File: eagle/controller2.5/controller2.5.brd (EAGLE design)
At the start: 63.5 x 45.7 mm, 46 parts, among them Q2 2N2907, U1 ATMEGA328P

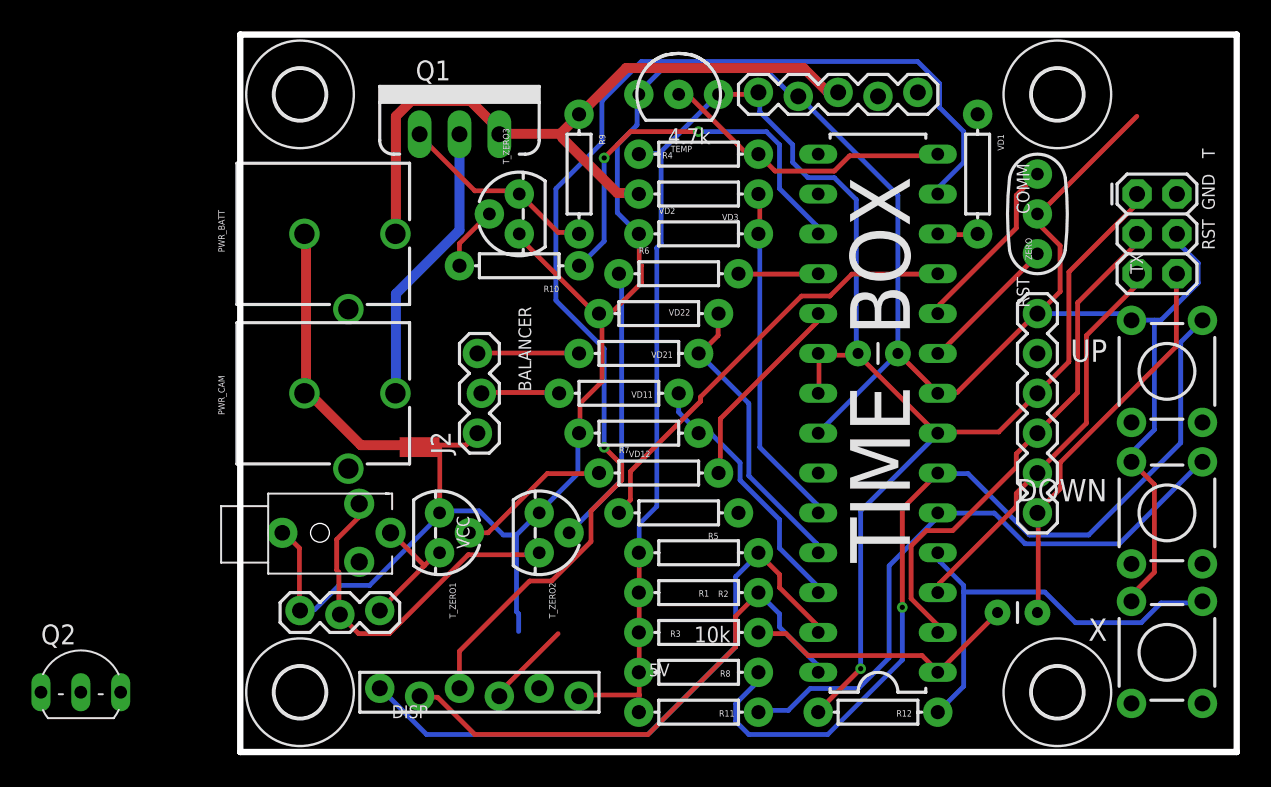
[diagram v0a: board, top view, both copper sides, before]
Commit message: controller2.5: smaller board
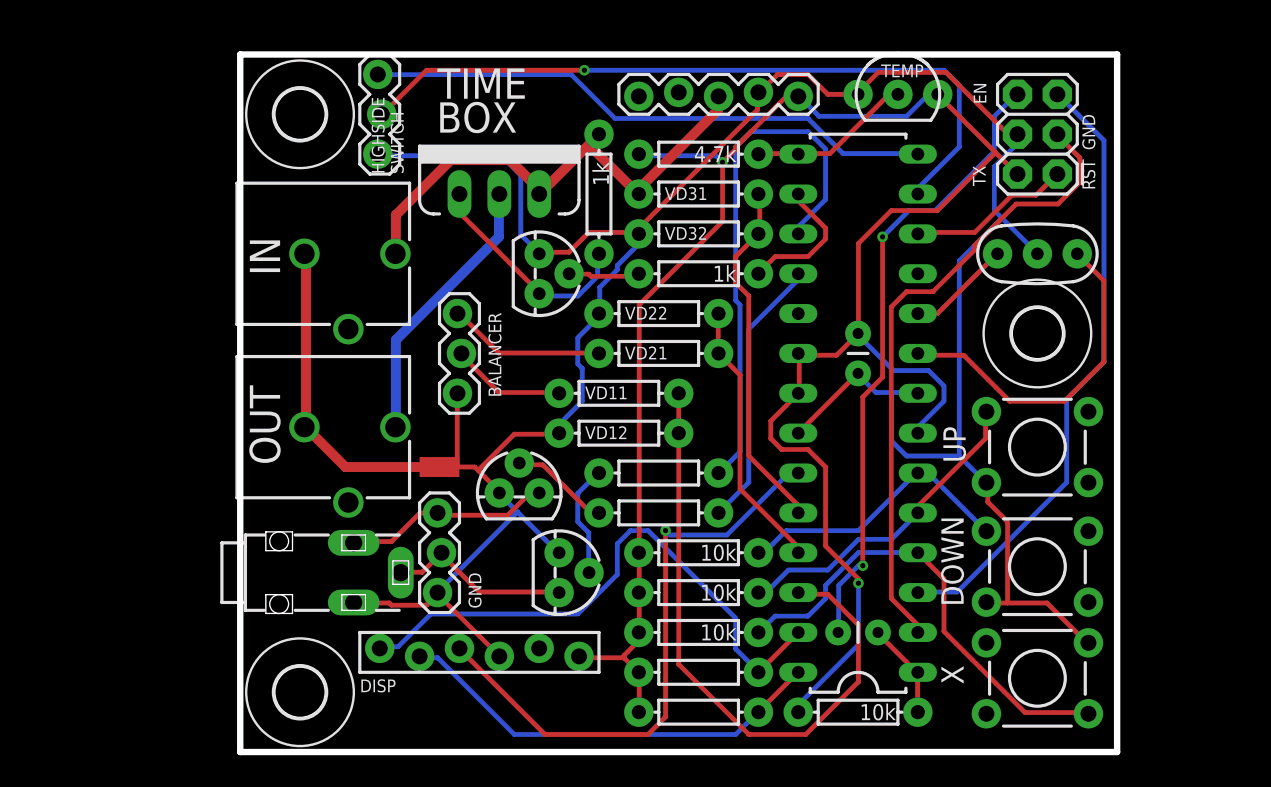
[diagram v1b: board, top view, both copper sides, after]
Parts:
- removed COMM: (no value), SparkFun-Connectors:FTDI_BASIC
- removed H2: MOUNT-HOLE3.2, holes:3,2
- removed J1: (no value), SparkFun-Connectors:STEREOJACK2.5MM_STEREOJACK2.5MM
- removed Q1: (no value), SparkFun-DiscreteSemi:TO220V
- removed Q2: 2N2907, adafruit:TO92-EBC-OVAL
- removed R11, R12, R5, R8, VD1: (no value), SparkFun-Resistors:AXIAL-0.3
- removed T_ZERO1, T_ZERO2, T_ZERO3: (no value), SparkFun-DiscreteSemi:TO-92
- added HIGHSIDESWITCH: (no value), SparkFun-DiscreteSemi:TO220V
- added RB1, RB2, RB3: 10k, SparkFun-Resistors:AXIAL-0.3
- added SOFT_SERIAL: (no value), SparkFun-Connectors:1X03_LOCK
- added T_CAM1, T_CAM2, T_HSS: (no value), SparkFun-DiscreteSemi:TO-92
- added X1: 1501_04, con-lumberg:1501_05
- R10, R9: value (none) -> 1k
- ZERO: value FEMALE 2x3 -> (none)
- moved H3 15.3 mm to (50.8, 26.7)
- moved BTN_UP 14.9 mm to (50.8, 11.8), turned to 180 degrees
- moved TEMP 14.0 mm to (41.9, 41.9)
- moved R6 12.8 mm to (26.7, 17.8)
- moved C1 12.8 mm to (38.1, 7.62), turned to 0 degrees
- moved R10 11.4 mm to (29.2, 30.5)
- moved R3 11.4 mm to (39.4, 2.54)
- moved BTN_DW 9.26 mm to (50.8, 19.4), turned to 180 degrees
- moved SHTR 8.98 mm to (12.7, 10.2), turned to 90 degrees
- moved BTN_X 8.42 mm to (50.8, 4.70), turned to 0 degrees
- moved R2 7.62 mm to (29.2, 2.54)
- moved R1 7.62 mm to (29.2, 5.08)
- moved ZERO 5.24 mm to (52.1, 36.8), turned to 90 degrees
- moved C3 2.84 mm to (39.4, 24.1), turned to 90 degrees
- moved J2 2.84 mm to (14.0, 22.9)
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- renumbered R4 to RTEMP, VD2 to VD32, VD3 to VD31
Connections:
- removed net EXT_EN: U1.15
- removed net FOO: U1.23
- removed net N$12: Q2.C, ZERO.1
- removed net N$4: Q2.B, VD1.P$1
- removed net N$6: DISP.4
- new net FOO2: U1.19
- new net SOFT_RX: SOFT_SERIAL.3, U1.14
- new net SOFT_TX: SOFT_SERIAL.2, U1.13
- net BATT_VCC: now also HIGHSIDESWITCH.3; no longer Q1.3
- net BTN1: now also RB1.P$1; no longer R8.P$1
- net BTN2: now also RB2.P$1; no longer R11.P$1
- net BTN3: now also RB3.P$1; no longer R12.P$1
- net CAM1: now also U1.18; no longer U1.19
- net CAM2: now also U1.17; no longer U1.18
- net CAM_EN: now also U1.16; no longer U1.17
- net CAM_OUT: now also HIGHSIDESWITCH.2; no longer Q1.2
- net DISP_RST: now also U1.23; no longer U1.13
- net GND: now also DISP.4, SOFT_SERIAL.1, T_CAM1.1, T_CAM2.1, T_HSS.1, X1.1; no longer COMM.GND, J1.SHIELD, T_ZERO1.1, T_ZERO2.1, T_ZERO3.1
- net N$10: now also T_CAM1.3, X1.3; no longer J1.TIP, T_ZERO1.3
- net N$11: now also T_CAM2.2; no longer T_ZERO2.2
- net N$13: now also T_HSS.2; no longer T_ZERO3.2
- net N$14: now also HIGHSIDESWITCH.1, T_HSS.3; no longer Q1.1, T_ZERO3.3
- net N$3: now also T_CAM1.2; no longer T_ZERO1.2
- net N$7: now also T_CAM2.3, X1.2; no longer J1.RING, T_ZERO2.3
- net RST: no longer COMM.DTR
- net RX: no longer COMM.TXO
- net TEMP: now also U1.15; no longer U1.14
- net TX: no longer COMM.RXI
- net VCC: now also RB1.P$2, RB2.P$2, RB3.P$2; no longer COMM.VCC, Q2.E, R11.P$2, R12.P$2, R8.P$2
- net ZERO_EN: now also ZERO.1; no longer VD1.P$2
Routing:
- net SOFT_TX: track 0.00 -> 46.4 mm, vias 0 -> 1
- net BTN1: track 57.4 -> 18.1 mm, vias 1 -> 0
- net DISP_RST: track 77.0 -> 38.0 mm
- net SOFT_RX: track 0.00 -> 36.5 mm
- net CAM2: track 5.09 -> 34.2 mm
- net DISP_EN: track 27.8 -> 0.00 mm
- net CELL1: track 16.8 -> 40.3 mm
- net BTN2: track 40.2 -> 20.5 mm
- net CAM_EN: track 26.5 -> 8.79 mm, vias 2 -> 0
- net RST: track 25.3 -> 40.2 mm, vias 0 -> 2
- net TX: track 25.6 -> 39.3 mm
- net BATT_VCC: track 46.1 -> 33.1 mm
- net N$9: track 9.07 -> 21.7 mm
- net N$1: track 17.9 -> 6.18 mm
- net N$7: track 23.1 -> 11.7 mm
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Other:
- board size 63.5 x 45.7 mm -> 55.9 x 44.5 mm
- board text added: "EN"
- board text added: "HIGHSIDE SWITCH"
- board text added: "IN"
- board text added: "OUT"
- board text added: "TEMP"
- board text added: "VD11"
- board text added: "VD12"
- board text added: "VD21"
- board text added: "VD22"
- board text added: "VD31"
- board text added: "VD32"
- board text removed: "5V"
- board text removed: "COMM"
- board text removed: "T"
- board text removed: "VCC"

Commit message: controller2.5: production version
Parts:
- moved SOFT_SERIAL 36.9 mm to (45.7, 36.8)
- moved RTEMP 18.2 mm to (45.7, 30.5), turned to 90 degrees
- moved C1 7.18 mm to (43.2, 2.54), turned to 180 degrees
- moved R3 5.08 mm to (34.3, 2.54)
- moved C3 3.81 mm to (39.4, 27.9), turned to 270 degrees
- moved VD22 3.59 mm to (29.2, 30.5)
- moved R10 2.54 mm to (29.2, 33.0)
- moved VD21 2.54 mm to (26.7, 27.9)
- moved R7 2.54 mm to (26.7, 17.8)
- moved RB1 2.54 mm to (29.2, 15.2)
- moved R1 2.54 mm to (29.2, 7.62)
- moved R2 2.54 mm to (29.2, 5.08)
- moved RB3 2.54 mm to (29.2, 10.2)
- moved R6 2.54 mm to (26.7, 20.3)
- moved RB2 2.54 mm to (29.2, 12.7)
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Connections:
- removed net DISP_EN: U1.11
- removed net FOO2: U1.19
- net CAM2: now also U1.16; no longer U1.17
- net CAM_EN: now also U1.17; no longer U1.16
- net SOFT_TX: now also U1.15; no longer U1.13
- net TEMP: now also U1.13; no longer U1.15
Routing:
- net VCC: track 130.9 -> 80.8 mm, vias 2 -> 0
- net TX: track 39.3 -> 87.2 mm
- net SOFT_TX: track 46.4 -> 10.9 mm, vias 1 -> 0
- net SOFT_RX: track 36.5 -> 4.88 mm
- net CAM2: track 34.2 -> 19.8 mm
- net RST: track 40.2 -> 51.4 mm, vias 2 -> 0
- net BTN3: track 29.8 -> 19.6 mm
- net TEMP: track 10.5 -> 20.7 mm
- net N$9: track 21.7 -> 11.8 mm
- net VD_DIRECT: track 22.6 -> 30.4 mm
- net N$8: track 6.65 -> 13.4 mm
- net CAM_EN: track 8.79 -> 2.57 mm
- net CELL2: track 17.4 -> 23.5 mm, vias 0 -> 1
- net GND: track 169.9 -> 175.4 mm
- net DISP_RST: track 38.0 -> 32.5 mm, vias 1 -> 0
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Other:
- board text added: "RX"
- board text added: "VIN"

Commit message: controller2.5: last minor changes for production
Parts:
- moved CONV_X_VCC 1.27 mm to (34.3, 41.9)
- moved TEMP 1.27 mm to (39.4, 41.9)
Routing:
- net TX: track 87.2 -> 78.1 mm
- net BATT_VCC: track 28.2 -> 26.9 mm
- net TEMP: track 20.7 -> 21.3 mm
- net VCC: track 80.8 -> 81.3 mm
